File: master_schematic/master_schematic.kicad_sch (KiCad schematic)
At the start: 4 parts, among them U1 teensy_4.1, U15 EA50 Power Converter, U2 RFM95

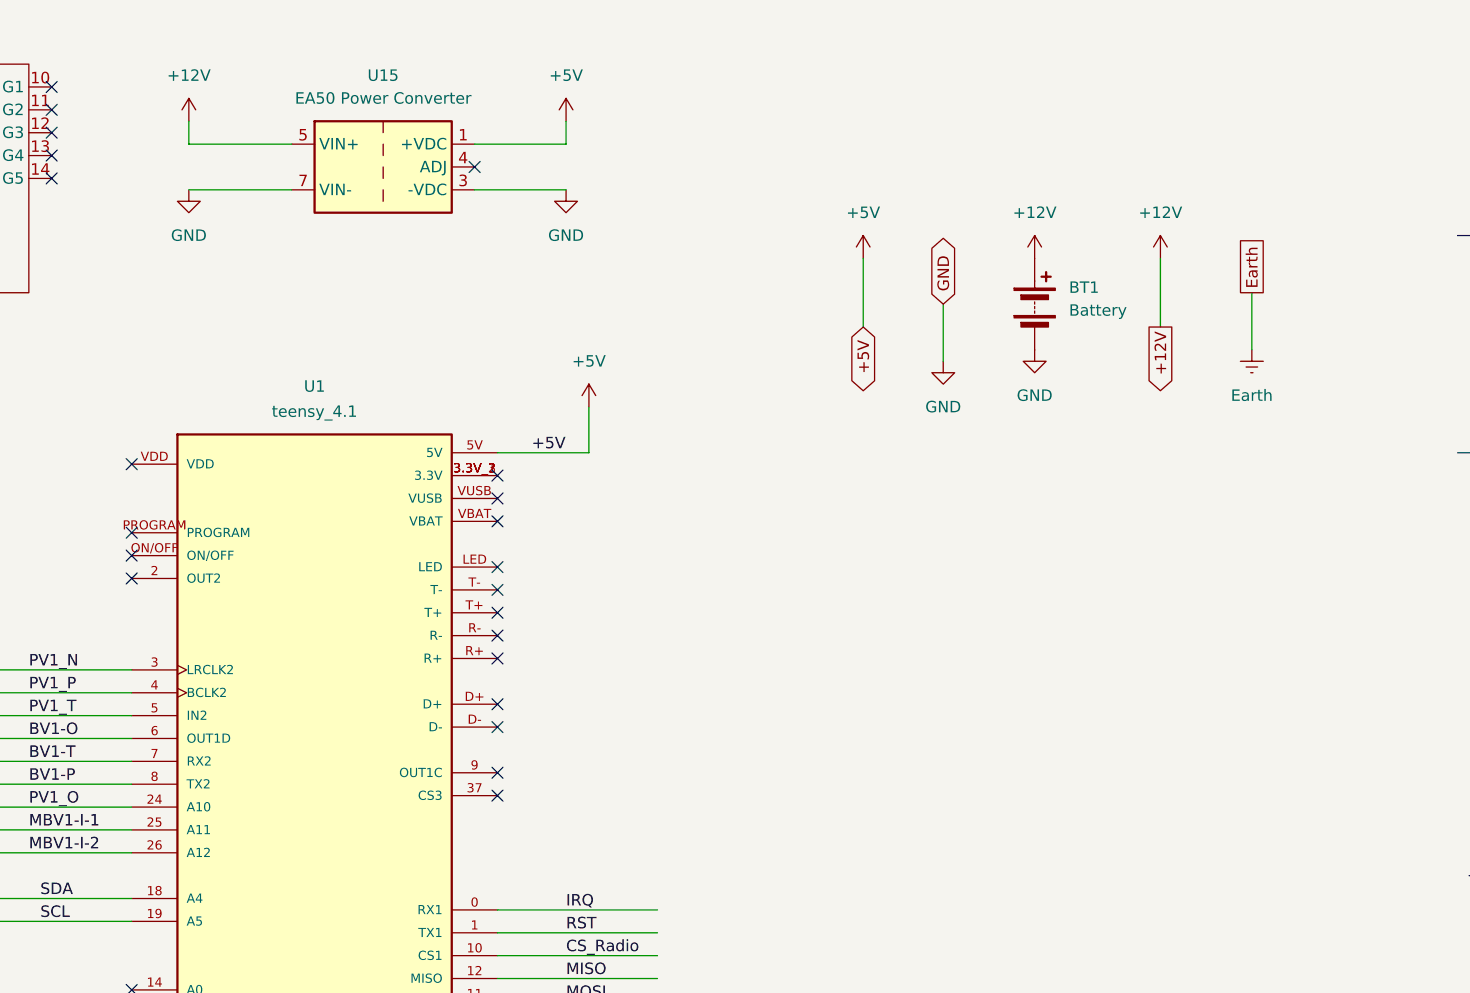
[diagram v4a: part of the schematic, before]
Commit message: updated with part info
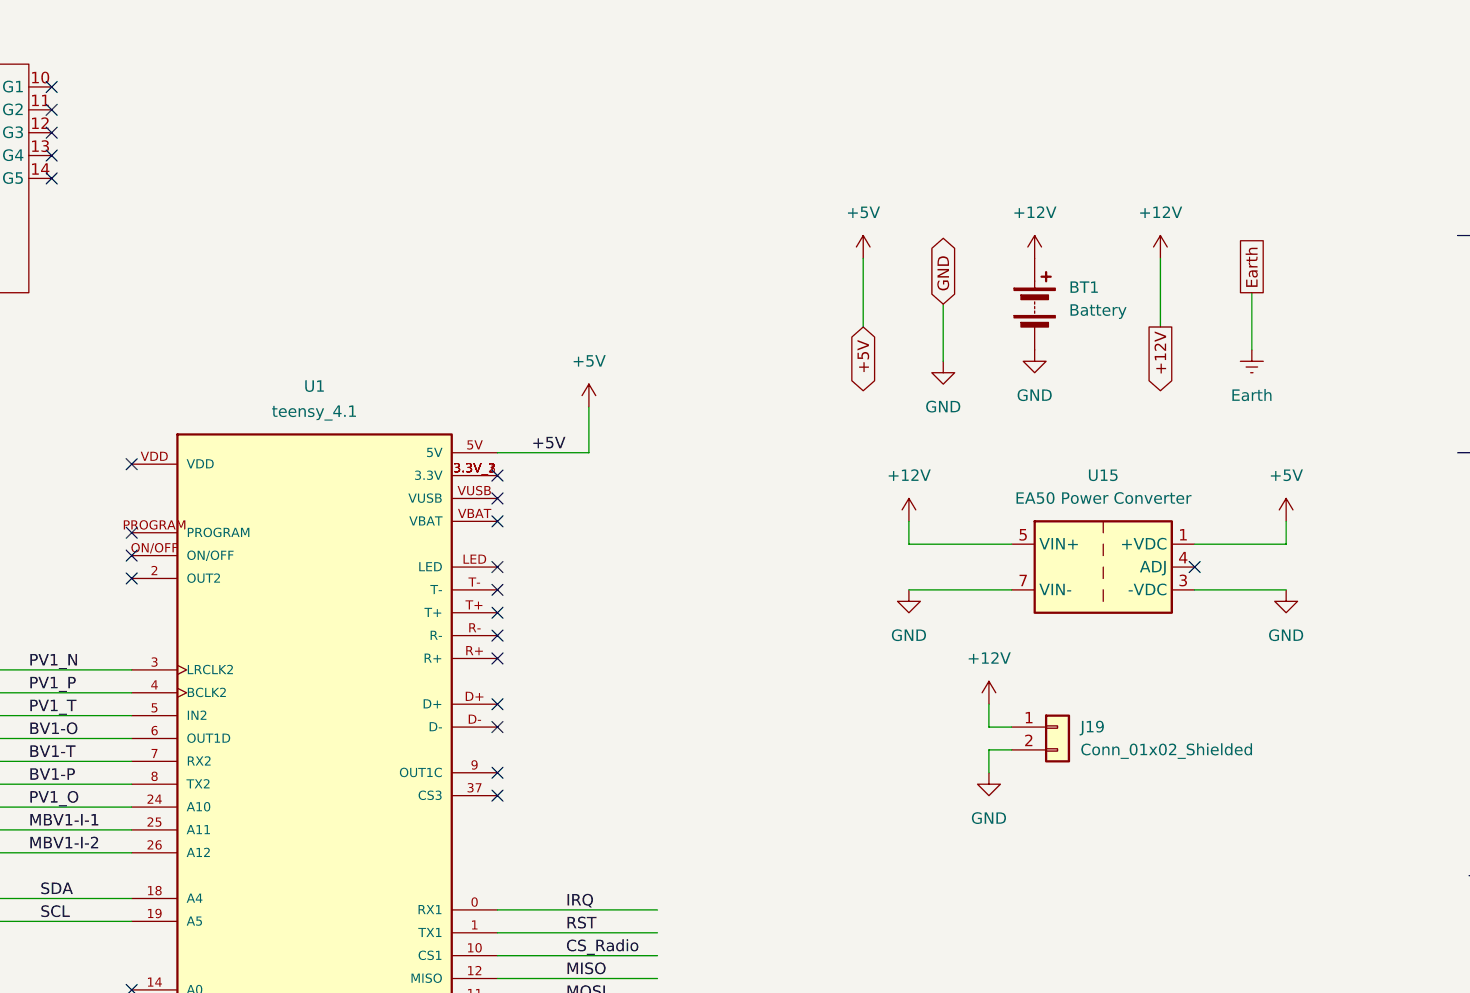
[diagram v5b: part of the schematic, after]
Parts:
- added J19: Conn_01x02_Shielded, hb_footprint_lib:AMASS_XT60PW-M, symbol Connector_Generic:Conn_01x02
- U1: now left out of the parts list
- U2: footprint hb_footprint_lib:Radio_Module -> hb_footprint_lib:rfm95_connector
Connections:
- net +12V: now also J19.1 (Pin_1)
- net GND: now also J19.2 (Pin_2)
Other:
- moved on the sheet: U15

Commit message: fixed errors on schematic
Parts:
- renumbered J19 to J1, U15 to U3
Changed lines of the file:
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@@
+		)
+	)
+	(label "{LC}"
+		(at 52.07 157.48 0)
+		(fields_autoplaced yes)
+		(effects
+			(font
+				(size 1.27 1.27)
+			)
+			(justify left bottom)
 		)
 	)
@@
 		(dnp no)
 		(fields_autoplaced yes)
-		(property "Reference" "#PWR01"
+		(property "Reference" "#PWR02"
 			(at 138.43 78.74 0)
 			(effects
@@
 		)
 		(instances
-			(project ""
+			(project "master_schematic"
 				(path "/c4f7e98c-e88d-49cc-9841-b70710a90a72"
-					(reference "#PWR01")
+					(reference "#PWR02")
 					(unit 1)
 				)
@@
 		(dnp no)
 		(fields_autoplaced yes)
-		(property "Reference" "#PWR028"
+		(property "Reference" "#PWR011"
 			(at 201.93 62.23 0)
 			(effects
@@
 			(project "master_schematic"
 				(path "/c4f7e98c-e88d-49cc-9841-b70710a90a72"
-					(reference "#PWR028")
+					(reference "#PWR011")
 					(unit 1)
 				)
@@
 		)
 		(instances
-			(project ""
+			(project "master_schematic"
 				(path "/c4f7e98c-e88d-49cc-9841-b70710a90a72"
 					(reference "BT1")
@@
 		(dnp no)
 		(fields_autoplaced yes)
-		(property "Reference" "#PWR049"
+		(property "Reference" "#PWR07"
 			(at 182.88 111.76 0)
 			(effects
@@
 		)
 		(instances
-			(project ""
+			(project "master_schematic"
 				(path "/c4f7e98c-e88d-49cc-9841-b70710a90a72"
-					(reference "#PWR049")
+					(reference "#PWR07")
 					(unit 1)
 				)
@@
 		(dnp no)
 		(fields_autoplaced yes)
-		(property "Reference" "#PWR027"
+		(property "Reference" "#PWR010"
 			(at 187.96 74.93 0)
 			(effects
@@
 			(project "master_schematic"
 				(path "/c4f7e98c-e88d-49cc-9841-b70710a90a72"
-					(reference "#PWR027")
+					(reference "#PWR010")
 					(unit 1)
 				)
@@
 		(dnp no)
 		(fields_autoplaced yes)
-		(property "Reference" "#PWR016"
+		(property "Reference" "#PWR06"
 			(at 177.8 76.2 0)
 			(effects
@@
 		)
 		(instances
-			(project ""
+			(project "master_schematic"
 				(path "/c4f7e98c-e88d-49cc-9841-b70710a90a72"
-					(reference "#PWR016")
+					(reference "#PWR06")
 					(unit 1)
 				)
@@
 		(dnp no)
 		(fields_autoplaced yes)
-		(property "Reference" "U15"
+		(property "Reference" "U3"
 			(at 195.58 82.55 0)
 			(effects
@@
 		)
 		(instances
-			(project ""
+			(project "master_schematic"
 				(path "/c4f7e98c-e88d-49cc-9841-b70710a90a72"
-					(reference "U15")
+					(reference "U3")
 					(unit 1)
 				)
@@
 		(dnp no)
 		(fields_autoplaced yes)
-		(property "Reference" "#PWR050"
+		(property "Reference" "#PWR08"
 			(at 182.88 121.92 0)
 			(effects
@@
 		)
 		(instances
-			(project ""
+			(project "master_schematic"
 				(path "/c4f7e98c-e88d-49cc-9841-b70710a90a72"
-					(reference "#PWR050")
+					(reference "#PWR08")
 					(unit 1)
 				)
@@
 		(fields_autoplaced yes)
 		(property "Reference" "U2"
-			(at 69.85 33.02 0)
+			(at 69.85 31.75 0)
 			(effects
 				(font
@@
 		)
 		(property "Value" "RFM95"
-			(at 69.85 35.56 0)
+			(at 69.85 34.29 0)
 			(effects
 				(font
@@
 		(dnp no)
 		(fields_autoplaced yes)
-		(property "Reference" "#PWR015"
+		(property "Reference" "#PWR01"
 			(at 135.89 182.88 0)
 			(effects
@@
 		)
 		(instances
-			(project ""
+			(project "master_schematic"
 				(path "/c4f7e98c-e88d-49cc-9841-b70710a90a72"
-					(reference "#PWR015")
+					(reference "#PWR01")
 					(unit 1)
 				)
@@
 		(dnp no)
 		(fields_autoplaced yes)
-		(property "Reference" "#PWR02"
+		(property "Reference" "#PWR03"
 			(at 168.91 62.23 0)
 			(effects
@@
 			(project "master_schematic"
 				(path "/c4f7e98c-e88d-49cc-9841-b70710a90a72"
-					(reference "#PWR02")
+					(reference "#PWR03")
 					(unit 1)
 				)
@@
 		(dnp no)
 		(fields_autoplaced yes)
-		(property "Reference" "#PWR026"
+		(property "Reference" "#PWR09"
 			(at 187.96 62.23 0)
 			(effects
@@
 		)
 		(instances
-			(project ""
+			(project "master_schematic"
 				(path "/c4f7e98c-e88d-49cc-9841-b70710a90a72"
-					(reference "#PWR026")
+					(reference "#PWR09")
 					(unit 1)
 				)
@@
 		(dnp no)
 		(fields_autoplaced yes)
-		(property "Reference" "#PWR038"
+		(property "Reference" "#PWR013"
 			(at 215.9 91.44 0)
 			(effects
@@
 			(project "master_schematic"
 				(path "/c4f7e98c-e88d-49cc-9841-b70710a90a72"
-					(reference "#PWR038")
+					(reference "#PWR013")
 					(unit 1)
 				)
@@
 		(dnp no)
 		(fields_autoplaced yes)
-		(property "Reference" "J19"
+		(property "Reference" "J1"
 			(at 193.04 110.4899 0)
 			(effects
@@
 		)
 		(instances
-			(project ""
+			(project "master_schematic"
 				(path "/c4f7e98c-e88d-49cc-9841-b70710a90a72"
-					(reference "J19")
+					(reference "J1")
 					(unit 1)
 				)
@@
 		(dnp no)
 		(fields_autoplaced yes)
-		(property "Reference" "#PWR036"
+		(property "Reference" "#PWR04"
 			(at 173.99 91.44 0)
 			(effects
@@
 		)
 		(instances
-			(project ""
+			(project "master_schematic"
 				(path "/c4f7e98c-e88d-49cc-9841-b70710a90a72"
-					(reference "#PWR036")
+					(reference "#PWR04")
 					(unit 1)
 				)
@@
 		(dnp no)
 		(fields_autoplaced yes)
-		(property "Reference" "#PWR037"
+		(property "Reference" "#PWR05"
 			(at 173.99 101.6 0)
 			(effects
@@
 		)
 		(instances
-			(project ""
+			(project "master_schematic"
 				(path "/c4f7e98c-e88d-49cc-9841-b70710a90a72"
-					(reference "#PWR037")
+					(reference "#PWR05")
 					(unit 1)
 				)
@@
 		(dnp no)
 		(fields_autoplaced yes)
-		(property "Reference" "#PWR039"
+		(property "Reference" "#PWR014"
 			(at 215.9 101.6 0)
 			(effects
@@
 			(project "master_schematic"
 				(path "/c4f7e98c-e88d-49cc-9841-b70710a90a72"
-					(reference "#PWR039")
+					(reference "#PWR014")
 					(unit 1)
 				)
@@
 		(dnp no)
 		(fields_autoplaced yes)
-		(property "Reference" "#PWR032"
+		(property "Reference" "#PWR012"
 			(at 212.09 74.93 0)
 			(effects
@@
 		)
 		(instances
-			(project ""
+			(project "master_schematic"
 				(path "/c4f7e98c-e88d-49cc-9841-b70710a90a72"
-					(reference "#PWR032")
+					(reference "#PWR012")
 					(unit 1)
 				)

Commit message: finished building PCB
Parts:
- added H1, H2, H3, H4: MountingHole, MountingHole:MountingHole_4.3mm_M4_DIN965_Pad, symbol Mechanical:MountingHole

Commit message: updated BOM
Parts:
- BT1, U3: now left out of the parts list
- U1: Availability In Stock -> (none); Check_prices https://www.snapeda.com/parts/DEV-16771/SparkFun+Electronic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 -> (none); Cost @ Qty (none) -> 1.75; Description_1 RT1062 Teensy 4.1 series ARM® Cortex®-M7 MPU Embedded Evalu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 -> (none); MANUFACTURER SparkFun Electronics -> (none); MAXIMUM_PACKAGE_HEIGHT 4.07mm -> (none); MF SparkFun Electronics -> (none); MP DEV-16771 -> (none); Manufacturer (none) -> SparkFun Electronics; Manufacturer Part # (none) -> PRT-17152; PARTREV 4.1 -> (none); Package None -> (none); Price None -> (none); STANDARD Manufacturer recommendations -> (none); SnapEDA_Link https://www.snapeda.com/parts/DEV-16771/SparkFun+Electronic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 -> (none); Supplier (none) -> Digikey; Supplier Part # (none) -> PRT-17152; Unit Cost (none) -> 1.75
- U2: Cost @ Qty (none) -> 0.63; Cost @ Qty 2 (none) -> 0.43; Manufacturer (none) -> Sullins Connector Solutions; Manufacturer 2 (none) -> Sullins Connector Solutions; Manufacturer Part # (none) -> PPPC091LFBN-RC; Manufacturer Part # 2 (none) -> PPPC051LFBN-RC; Supplier (none) -> Digikey; Supplier 2 (none) -> Digikey; Supplier Part # (none) -> PPPC091LFBN-RC; Supplier Part # 2 (none) -> PPPC051LFBN-RC; Unit Cost (none) -> 0.63; Unit Cost 2 (none) -> 0.43
